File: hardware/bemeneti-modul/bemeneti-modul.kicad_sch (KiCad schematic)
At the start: 0 parts

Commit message: Hardver: bemeneti modul kapcsolási rajz + HDC3020 + buszos táp opció
16 bemenet JST-PH-n (1k + 10k felhúzás + 10 nF, osztó-footprint, ESD),
4 érzékelő-tápcsoport (3,3 / 5 V forrasztható választó + PTC, külön NCP1117),
HDC3020 (saját szimbólum + DEF0008A footprint) + külső I²C PH-csatlakozó.
Modulmag: opcionális buszos táp (D6 + JP2, alapból üres) – D66. ERC: 0 hiba.

Co-Authored-By: Claude Opus 5.5 <noreply@anthropic.com>
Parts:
- added C301, C320: 100n, Capacitor_SMD:C_0603_1608Metric, symbol Device:C
- added C302: 10µ/10V, Capacitor_SMD:C_0805_2012Metric, symbol Device:C
- added C303: 10µ tantál, Capacitor_Tantalum_SMD:CP_EIA-3216-18_Kemet-A, symbol Device:C_Polarized
- added C304, C305, C306, C307: 1µ, Capacitor_SMD:C_0603_1608Metric, symbol Device:C
- added C310, C311, C312, C313, C314, C315, C316, C317, C318, C319, C320, C321, C322, C323, C324, C325: 10n, Capacitor_SMD:C_0603_1608Metric, symbol Device:C
- added F301, F302, F303, F304, F305: PTC 0,2A, Fuse:Fuse_1206_3216Metric, symbol Device:Polyfuse
- added J300: 24V IN, TerminalBlock_Phoenix:TerminalBlock_Phoenix_PT-1,5-2-5.0-H_1x02_P5.00mm_Horizontal, symbol Connector_Generic:Conn_01x02
- added J301: IN0, Connector_JST:JST_PH_B3B-PH-K_1x03_P2.00mm_Vertical, symbol Connector_Generic:Conn_01x03
- added J302: IN1, Connector_JST:JST_PH_B3B-PH-K_1x03_P2.00mm_Vertical, symbol Connector_Generic:Conn_01x03
- added J303: IN2, Connector_JST:JST_PH_B3B-PH-K_1x03_P2.00mm_Vertical, symbol Connector_Generic:Conn_01x03
- added J304: IN3, Connector_JST:JST_PH_B3B-PH-K_1x03_P2.00mm_Vertical, symbol Connector_Generic:Conn_01x03
- added J305: IN4, Connector_JST:JST_PH_B3B-PH-K_1x03_P2.00mm_Vertical, symbol Connector_Generic:Conn_01x03
- added J306: IN5, Connector_JST:JST_PH_B3B-PH-K_1x03_P2.00mm_Vertical, symbol Connector_Generic:Conn_01x03
- added J307: IN6, Connector_JST:JST_PH_B3B-PH-K_1x03_P2.00mm_Vertical, symbol Connector_Generic:Conn_01x03
- added J308: IN7, Connector_JST:JST_PH_B3B-PH-K_1x03_P2.00mm_Vertical, symbol Connector_Generic:Conn_01x03
- added J309: IN8, Connector_JST:JST_PH_B3B-PH-K_1x03_P2.00mm_Vertical, symbol Connector_Generic:Conn_01x03
- added J310: IN9, Connector_JST:JST_PH_B3B-PH-K_1x03_P2.00mm_Vertical, symbol Connector_Generic:Conn_01x03
- added J311: IN10, Connector_JST:JST_PH_B3B-PH-K_1x03_P2.00mm_Vertical, symbol Connector_Generic:Conn_01x03
- added J312: IN11, Connector_JST:JST_PH_B3B-PH-K_1x03_P2.00mm_Vertical, symbol Connector_Generic:Conn_01x03
- added J313: IN12, Connector_JST:JST_PH_B3B-PH-K_1x03_P2.00mm_Vertical, symbol Connector_Generic:Conn_01x03
- added J314: IN13, Connector_JST:JST_PH_B3B-PH-K_1x03_P2.00mm_Vertical, symbol Connector_Generic:Conn_01x03
- added J315: IN14, Connector_JST:JST_PH_B3B-PH-K_1x03_P2.00mm_Vertical, symbol Connector_Generic:Conn_01x03
- added J316: IN15, Connector_JST:JST_PH_B3B-PH-K_1x03_P2.00mm_Vertical, symbol Connector_Generic:Conn_01x03
- added J320: I2C KÜLSŐ, Connector_JST:JST_PH_B4B-PH-K_1x04_P2.00mm_Vertical, symbol Connector_Generic:Conn_01x04
- added JP301: CSOPORT 1, Jumper:SolderJumper-3_P1.3mm_Bridged12_RoundedPad1.0x1.5mm, symbol Jumper:SolderJumper_3_Bridged12
- added JP302: CSOPORT 2, Jumper:SolderJumper-3_P1.3mm_Bridged12_RoundedPad1.0x1.5mm, symbol Jumper:SolderJumper_3_Bridged12
- added JP303: CSOPORT 3, Jumper:SolderJumper-3_P1.3mm_Bridged12_RoundedPad1.0x1.5mm, symbol Jumper:SolderJumper_3_Bridged12
- added JP304: CSOPORT 4, Jumper:SolderJumper-3_P1.3mm_Bridged12_RoundedPad1.0x1.5mm, symbol Jumper:SolderJumper_3_Bridged12
- added R301: 3k3 1%, Resistor_SMD:R_0603_1608Metric, symbol Device:R
- added R302: 10k 1%, Resistor_SMD:R_0603_1608Metric, symbol Device:R
- added R310, R311, R312, R313, R314, R315, R316, R317, R318, R319, R320, R321, R322, R323, R324, R325: 1k, Resistor_SMD:R_0603_1608Metric, symbol Device:R
- added R330, R331, R332, R333, R334, R335, R336, R337, R338, R339, R340, R341, R342, R343, R344, R345, R373: 10k, Resistor_SMD:R_0603_1608Metric, symbol Device:R
- added R350, R351, R352, R353, R354, R355, R356, R357, R358, R359, R360, R361, R362, R363, R364, R365: DNP, Resistor_SMD:R_0603_1608Metric, symbol Device:R
- added R371, R372: 4k7, Resistor_SMD:R_0603_1608Metric, symbol Device:R
- added R374, R375: 100R, Resistor_SMD:R_0603_1608Metric, symbol Device:R
- added U301: NCP1117ST33T3G, Package_TO_SOT_SMD:SOT-223-3_TabPin2, symbol Regulator_Linear:NCP1117-3.3_SOT223
- added U302: HDC3020DEFR, modularis:TI_WSON-8-1EP_2.5x2.5mm_DEF0008A, symbol modularis:HDC3020
- added U303, U304, U305, U306, U307: TPD4E05U06DQAR, Package_SON:USON-10_2.5x1.0mm_P0.5mm, symbol Power_Protection:TPD4E05U06DQA
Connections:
- new net +24V_IN: J300.1 (Pin_1)
- new net +3V3: C320.1, R301.1, R330.1, R331.1, R332.1, R333.1, R334.1, R335.1, R336.1, R337.1, R338.1, R339.1, R340.1, R341.1, R342.1, R343.1, R344.1, R345.1, R371.1, R372.1, R373.1, U302.5 (VDD), U302.6 (~{RESET})
- new net +3V3S: C303.1, F305.1, JP301.1 (A), JP302.1 (A), JP303.1 (A), JP304.1 (A), U301.2 (VO)
- new net +5V: C302.1, JP301.3 (B), JP302.3 (B), JP303.3 (B), JP304.3 (B), U301.3 (VI)
- new net GND: C301.2, C302.2, C303.2, C304.2, C305.2, C306.2, C307.2, C310.2, C311.2, C312.2, C313.2, C314.2, C315.2, C316.2, C317.2, C318.2, C319.2, C320.2, C320.2, C321.2, C322.2, C323.2, C324.2, C325.2, J300.2 (Pin_2), J301.2 (Pin_2), J302.2 (Pin_2), J303.2 (Pin_2), J304.2 (Pin_2), J305.2 (Pin_2), J306.2 (Pin_2), J307.2 (Pin_2), J308.2 (Pin_2), J309.2 (Pin_2), J310.2 (Pin_2), J311.2 (Pin_2), J312.2 (Pin_2), J313.2 (Pin_2), J314.2 (Pin_2), J315.2 (Pin_2), J316.2 (Pin_2), J320.2 (Pin_2), R302.2, R350.2, R351.2, R352.2, R353.2, R354.2, R355.2, R356.2, R357.2, R358.2, R359.2, R360.2, R361.2, R362.2, R363.2, R364.2, R365.2, U301.1 (GND), U302.2 (ADDR), U302.7 (ADDR1), U302.8 (GND), U303.3 (GND), U303.8 (GND), U304.3 (GND), U304.8 (GND), U305.3 (GND), U305.8 (GND), U306.3 (GND), U306.8 (GND), U307.3 (GND), U307.8 (GND)
- new net HDC_ALERT: R373.2, U302.3 (ALERT)
- new net HW_ID: C301.1, R301.2, R302.1
- new net I2C_SCL: R371.2, R374.1, U302.4 (SCL)
- new net I2C_SDA: R372.2, R375.1, U302.1 (SDA)
- new net IN0: C310.1, R310.2, R330.2, R350.1, U303.1 (D1+)
- new net IN0_EXT: J301.3 (Pin_3), R310.1
- new net IN1: C311.1, R311.2, R331.2, R351.1, U303.2 (D1-)
- new net IN10: C320.1, R320.2, R340.2, R360.1, U305.4 (D2+)
- new net IN10_EXT: J311.3 (Pin_3), R320.1
- new net IN11: C321.1, R321.2, R341.2, R361.1, U305.5 (D2-)
- new net IN11_EXT: J312.3 (Pin_3), R321.1
- new net IN12: C322.1, R322.2, R342.2, R362.1, U306.1 (D1+)
- new net IN12_EXT: J313.3 (Pin_3), R322.1
- new net IN13: C323.1, R323.2, R343.2, R363.1, U306.2 (D1-)
- new net IN13_EXT: J314.3 (Pin_3), R323.1
- new net IN14: C324.1, R324.2, R344.2, R364.1, U306.4 (D2+)
- new net IN14_EXT: J315.3 (Pin_3), R324.1
- new net IN15: C325.1, R325.2, R345.2, R365.1, U306.5 (D2-)
- new net IN15_EXT: J316.3 (Pin_3), R325.1
- new net IN1_EXT: J302.3 (Pin_3), R311.1
- new net IN2: C312.1, R312.2, R332.2, R352.1, U303.4 (D2+)
- new net IN2_EXT: J303.3 (Pin_3), R312.1
- new net IN3: C313.1, R313.2, R333.2, R353.1, U303.5 (D2-)
- new net IN3_EXT: J304.3 (Pin_3), R313.1
- new net IN4: C314.1, R314.2, R334.2, R354.1, U304.1 (D1+)
- new net IN4_EXT: J305.3 (Pin_3), R314.1
- new net IN5: C315.1, R315.2, R335.2, R355.1, U304.2 (D1-)
- new net IN5_EXT: J306.3 (Pin_3), R315.1
- new net IN6: C316.1, R316.2, R336.2, R356.1, U304.4 (D2+)
- new net IN6_EXT: J307.3 (Pin_3), R316.1
- new net IN7: C317.1, R317.2, R337.2, R357.1, U304.5 (D2-)
- new net IN7_EXT: J308.3 (Pin_3), R317.1
- new net IN8: C318.1, R318.2, R338.2, R358.1, U305.1 (D1+)
- new net IN8_EXT: J309.3 (Pin_3), R318.1
- new net IN9: C319.1, R319.2, R339.2, R359.1, U305.2 (D1-)
- new net IN9_EXT: J310.3 (Pin_3), R319.1
- new net SCL_EXT: J320.4 (Pin_4), R374.2, U307.1 (D1+)
- new net SDA_EXT: J320.3 (Pin_3), R375.2, U307.2 (D1-)
- new net SUP1: C304.1, F301.2, J301.1 (Pin_1), J302.1 (Pin_1), J303.1 (Pin_1), J304.1 (Pin_1)
- new net SUP1_SEL: F301.1, JP301.2 (C)
- new net SUP2: C305.1, F302.2, J305.1 (Pin_1), J306.1 (Pin_1), J307.1 (Pin_1), J308.1 (Pin_1)
- new net SUP2_SEL: F302.1, JP302.2 (C)
- new net SUP3: C306.1, F303.2, J309.1 (Pin_1), J310.1 (Pin_1), J311.1 (Pin_1), J312.1 (Pin_1)
- new net SUP3_SEL: F303.1, JP303.2 (C)
- new net SUP4: C307.1, F304.2, J313.1 (Pin_1), J314.1 (Pin_1), J315.1 (Pin_1), J316.1 (Pin_1)
- new net SUP4_SEL: F304.1, JP304.2 (C)
- new net SUP_I2C: F305.2, J320.1 (Pin_1)
- no-connect marks 0 -> 29
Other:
- added sheet modulmag (../modulmag/modulmag.kicad_sch)
- note added: "1. ÉRZÉKELŐ-TÁP: külön 3,3 V-os sín (U301, NCP1117) az 5 V-ról – egy zárlatos érzékelő nem indítja újra az MCU-t"
- note added: "2. BEMENETEK (× 16): PH-csatlakozó 1 = táp (SUPk), 2 = GND, 3 = JEL → R_s → MCU-láb; R_fel 3,3 V-ra, R_le (DNP) és C a GND-re, ESD az MCU-oldalon"
- note added: "3. HŐMÉRSÉKLET / PÁRATARTALOM: HDC3020 a NYÁK szélén (alatta és körülötte marás), + 4 tűs PH külső érzékelőhöz (D66)"
- note added: "4 csoport × 4 csatlakozó: csoportonként 3 padas forrasztható választó (alap: 3,3 V; átforrasztva: 5 V) + saját PTC"
- note added: "5 V-os csoportban az érzékelő jele is 5 V lehet: az IN8–IN10 (PA8–PA10) 5 V-tűrő, a többi bemeneten az osztó-footprint kell (R_s 2k2, R_le 3k9, R_fel ki)"
- note added: "Alap: R_s 1k + R_fel 10k + C 10n → érintkező, reed, gomb, open-drain (pl. AH1911), 3,3 V-os kimenet. 12/24 V-os jel: R_s 68k, R_le 10k, R_fel ki."
- note added: "ESD: 4 × TPD4E05U06 – a csatlakozók mellé,"
- note added: "HW-ID: bemeneti modul = 6. sáv (2,48 V)"
- note added: "MODULMAG – A változat, saját 24 V"
- note added: "P78E05 → NCP1117, izolált CAN (D66)"
- note added: "VÁZLAT – generálva a D44/D48/D51/D66 alapján (2026-10-16). Elrendezést rendezd; a bekötés címkékkel kész."
- note added: "a soros R MCU-oldalára"
- title: Általános bemeneti modul (16 bemenet) -> Bemeneti modul – 16 bemenet (JST-PH), 4 érzékelő-tápcsoport, HDC3020, modulmag

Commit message: Hardver: mind az öt kapcsolási rajz elrendezve (vezetékes, blokkos), netlista-ellenőrzővel
Funkcionális blokkok, balról jobbra jelút, tápsín felül / GND alul; blokkon belül
vezeték, blokkok között és az IC-lábakon címke. kigen: lábpozíció, place(),
wire/junction/rail, tükrözés, 1,27 mm-es rács, olvasható mezők. gen/netcmp.py:
két netlista lábszintű összevetése – a bekötés az átrendezés előttivel azonos
(a modulmag D66-os D6/JP2-jét kivéve). ERC: 0 hiba mind az öt lapon.

Co-Authored-By: Claude Opus 5.5 <noreply@anthropic.com>
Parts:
- removed C320: 10n, Capacitor_SMD:C_0603_1608Metric, symbol Device:C
- removed C320: 100n, Capacitor_SMD:C_0603_1608Metric, symbol Device:C
- added C320: 100n, Capacitor_SMD:C_0603_1608Metric, symbol Device:C
- added C320: 10n, Capacitor_SMD:C_0603_1608Metric, symbol Device:C
- U302: Megjegyzés I²C-cím 0x44 (ADDR = ADDR1 = GND); a külső érzékelő más cím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 -> (none)
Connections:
- net +3V3: now also C320.1
- net GND: now also C320.2, C320.2
- net IN10: now also C320.1
- net IN0_EXT: no longer names the net of J301.3 (Pin_3), R310.1
- net IN10_EXT: no longer names the net of J311.3 (Pin_3), R320.1
- net IN11_EXT: no longer names the net of J312.3 (Pin_3), R321.1
- net IN12_EXT: no longer names the net of J313.3 (Pin_3), R322.1
- net IN13_EXT: no longer names the net of J314.3 (Pin_3), R323.1
- net IN14_EXT: no longer names the net of J315.3 (Pin_3), R324.1
- net IN15_EXT: no longer names the net of J316.3 (Pin_3), R325.1
- net IN1_EXT: no longer names the net of J302.3 (Pin_3), R311.1
- net IN2_EXT: no longer names the net of J303.3 (Pin_3), R312.1
- net IN3_EXT: no longer names the net of J304.3 (Pin_3), R313.1
- net IN4_EXT: no longer names the net of J305.3 (Pin_3), R314.1
- net IN5_EXT: no longer names the net of J306.3 (Pin_3), R315.1
- net IN6_EXT: no longer names the net of J307.3 (Pin_3), R316.1
- net IN7_EXT: no longer names the net of J308.3 (Pin_3), R317.1
- net IN8_EXT: no longer names the net of J309.3 (Pin_3), R318.1
- net IN9_EXT: no longer names the net of J310.3 (Pin_3), R319.1
- net SUP1_SEL: no longer names the net of F301.1, JP301.2 (C)
- net SUP2_SEL: no longer names the net of F302.1, JP302.2 (C)
- net SUP3_SEL: no longer names the net of F303.1, JP303.2 (C)
- net SUP4_SEL: no longer names the net of F304.1, JP304.2 (C)
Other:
- note added: "1. ÉRZÉKELŐ-TÁP: külön 3,3 V-os sín (U301, NCP1117) az 5 V-ról – egy zárlatos érzékelő nem indítja újra az MCU-t;"
- note added: "2. BEMENETEK (× 16): PH 1 = táp (SUPk), 2 = GND, 3 = JEL → R_s → csomópont (R_fel a 3,3 V-ra, R_le (DNP) és C a GND-re) → MCU; ESD az MCU-oldalon (lent)"
- note added: "24 V betáp (J300)"
- note added: "3. HŐMÉRSÉKLET / PÁRATARTALOM:"
- note added: "4 csoport × 4 csatlakozó: csoportonként 3 padas forrasztható választó (alap 1–2 = 3,3 V; átforrasztva 2–3 = 5 V) + saját PTC (0,2 A)"
- note added: "5 V-os csoportban az érzékelő jele is 5 V lehet: az IN8–IN10 (PA8–PA10) 5 V-tűrő, a többi bemeneten az osztó-hely kell (R_s 2k2, R_le 3k9, R_fel ki)"
- note added: "= GND); a külső más címen. Az EP lebegve."
- note added: "ESD: 4 × TPD4E05U06 – a csatlakozók mellé, a soros R MCU-oldalára (a soros R korlátozza a magasabb feszültség áramát)"
- note added: "Generálva (hardware/gen/bemeneti-modul.py) – D44/D48/D51/D66 alapján; kézi szerkesztés helyett a generátort módosítsd."
- note added: "HDC3020 a NYÁK szélén (marással) + 4 tűs PH"
- note added: "IN0–IN3"
- note added: "IN12–IN15"
- note added: "IN4–IN7"
- note added: "IN8–IN11"
- note added: "KÜLSŐ I²C (J320)"
- note added: "külső érzékelőhöz (D66). Cím 0x44 (ADDR = ADDR1"
- note removed: "1. ÉRZÉKELŐ-TÁP: külön 3,3 V-os sín (U301, NCP1117) az 5 V-ról – egy zárlatos érzékelő nem indítja újra az MCU-t"
- note removed: "2. BEMENETEK (× 16): PH-csatlakozó 1 = táp (SUPk), 2 = GND, 3 = JEL → R_s → MCU-láb; R_fel 3,3 V-ra, R_le (DNP) és C a GND-re, ESD az MCU-oldalon"
- note removed: "3. HŐMÉRSÉKLET / PÁRATARTALOM: HDC3020 a NYÁK szélén (alatta és körülötte marás), + 4 tűs PH külső érzékelőhöz (D66)"
- note removed: "4 csoport × 4 csatlakozó: csoportonként 3 padas forrasztható választó (alap: 3,3 V; átforrasztva: 5 V) + saját PTC"
- note removed: "5 V-os csoportban az érzékelő jele is 5 V lehet: az IN8–IN10 (PA8–PA10) 5 V-tűrő, a többi bemeneten az osztó-footprint kell (R_s 2k2, R_le 3k9, R_fel ki)"
- note removed: "ESD: 4 × TPD4E05U06 – a csatlakozók mellé,"
- note removed: "VÁZLAT – generálva a D44/D48/D51/D66 alapján (2026-10-16). Elrendezést rendezd; a bekötés címkékkel kész."
- note removed: "a soros R MCU-oldalára"

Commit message: Hardver: kapcsolási rajzok olvashatósága (KiCad MCP vizuális ellenőrzés alapján), output/ gitignore
Co-Authored-By: Claude Opus 5.5 <noreply@anthropic.com>
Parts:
- removed C320: 100n, Capacitor_SMD:C_0603_1608Metric, symbol Device:C
- removed C320: 10n, Capacitor_SMD:C_0603_1608Metric, symbol Device:C
- added C320: 10n, Capacitor_SMD:C_0603_1608Metric, symbol Device:C
- added C320: 100n, Capacitor_SMD:C_0603_1608Metric, symbol Device:C
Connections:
- net +3V3: now also C320.1
- net GND: now also C320.2, C320.2
- net IN10: now also C320.1

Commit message: Hardver: átnézés (C320 javítva), LoRa-előkészítés (D68), bővítők (D69), R6/R7 = 0 Ω (D70)
- bemeneti modul: a HDC3020 hidegítője C330 lett (a C320 kétszer szerepelt);
  a generátor mostantól hibát dob duplikált jelölésre
- vezérlő: E22-900M22S LoRa + u.FL + 74LVC1G04, minden DNP; J8 bővítő (GPIO5),
  7 mérőpont; spec szerinti DNP-k (USB C, 1 MΩ, PMODE, CAN-fojtó + áthidalók);
  saját footprint az LMR36015-höz (RNX) és az E22-höz
- modulmag: HW_REV osztó (PB0), DNP J4 2 × 5 bővítő; relé: DNP SCT-013 → PA0
- mind az öt lap vizuálisan rendbe téve; R6/R7 = 0 Ω
- specek és döntésnapló frissítve (D68–D70)

Co-Authored-By: Claude Opus 5.5 <noreply@anthropic.com>
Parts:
- removed C320: 10n, Capacitor_SMD:C_0603_1608Metric, symbol Device:C
- removed C320: 100n, Capacitor_SMD:C_0603_1608Metric, symbol Device:C
- added C320: 10n, Capacitor_SMD:C_0603_1608Metric, symbol Device:C
- added C330: 100n, Capacitor_SMD:C_0603_1608Metric, symbol Device:C
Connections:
- net +3V3: now also C330.1
- net GND: now also C320.2, C330.2
- net IN10: now also C320.1
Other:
- title: Bemeneti modul – 16 bemenet (JST-PH), 4 érzékelő-tápcsoport, HDC3020, modulmag -> Bemeneti modul – 16 bemenet, 4 tápcsoport, HDC3020

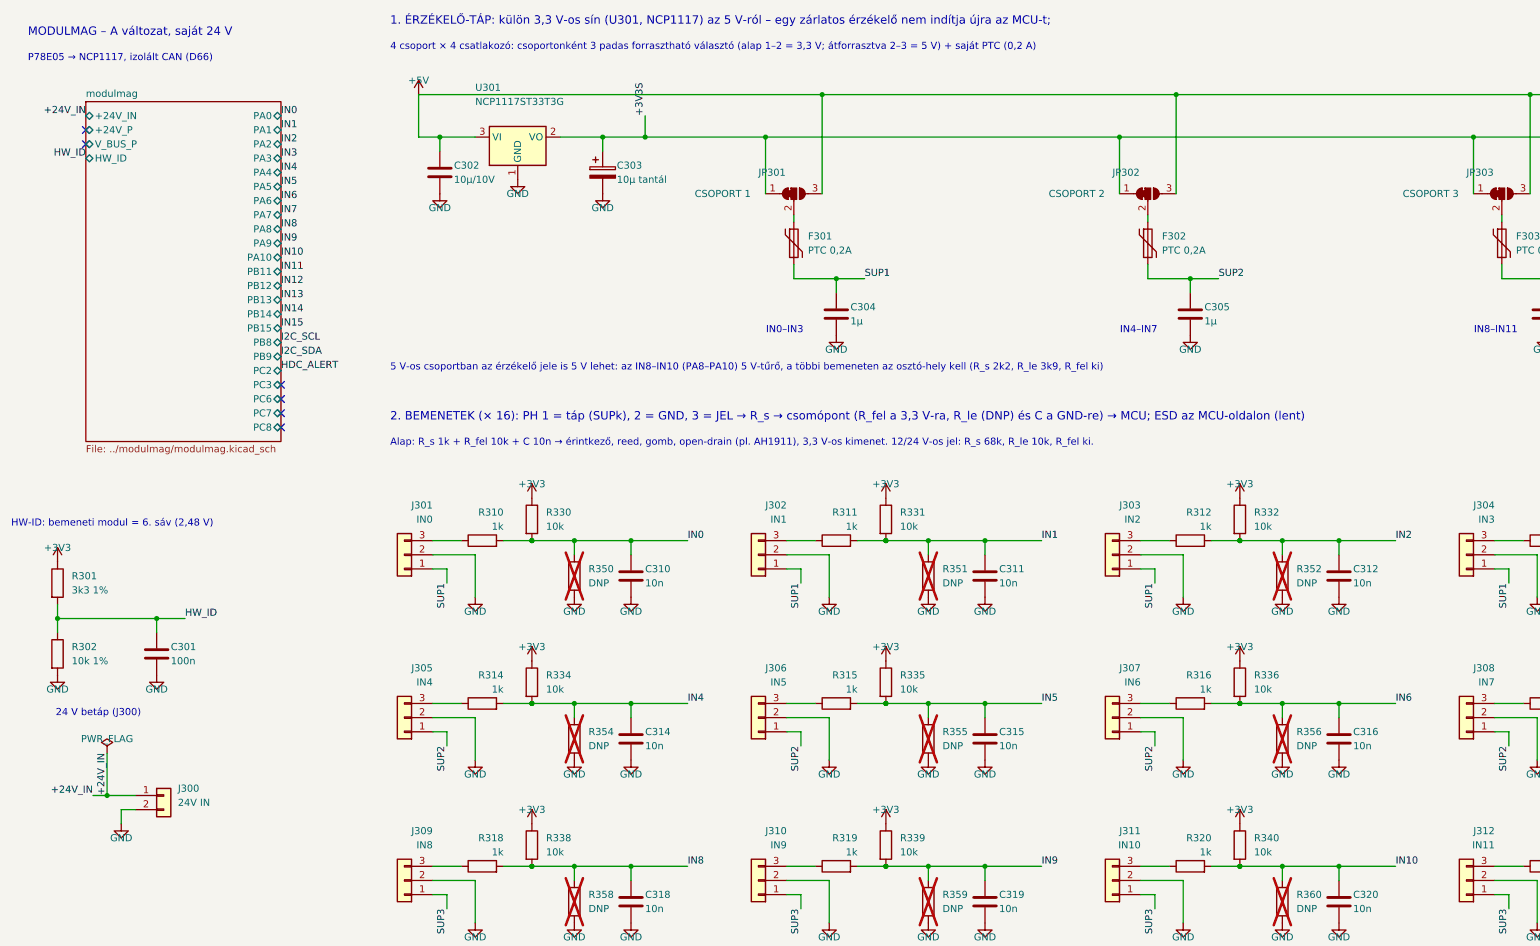
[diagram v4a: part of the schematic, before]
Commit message: Hardver: központi 5 V, közös föld, 12–26 V, HW-ID 16 sáv (D71)
Vezérlő: LMR33630 (5,2 V) + LM66200 (USB-vel VAGY-olva) + TPS259531 eFuse (2 A);
F1 2 A, D1 B360 a 12 V-os működéshez. Modulmag: táp a buszról (AP2112K), TCAN1044AV,
nincs izoláció, PC1 = VBUS_SENSE. LED/relé: VIN_SENSE a PB11-en, relémodul saját
tekercs-táppal. Bemeneti modul: nincs 24 V. HW-ID/HW_REV 16 sáv. Specifikációk,
áttekintés, beszerzés, ütemterv frissítve.

Co-Authored-By: Claude Opus 5.5 <noreply@anthropic.com>
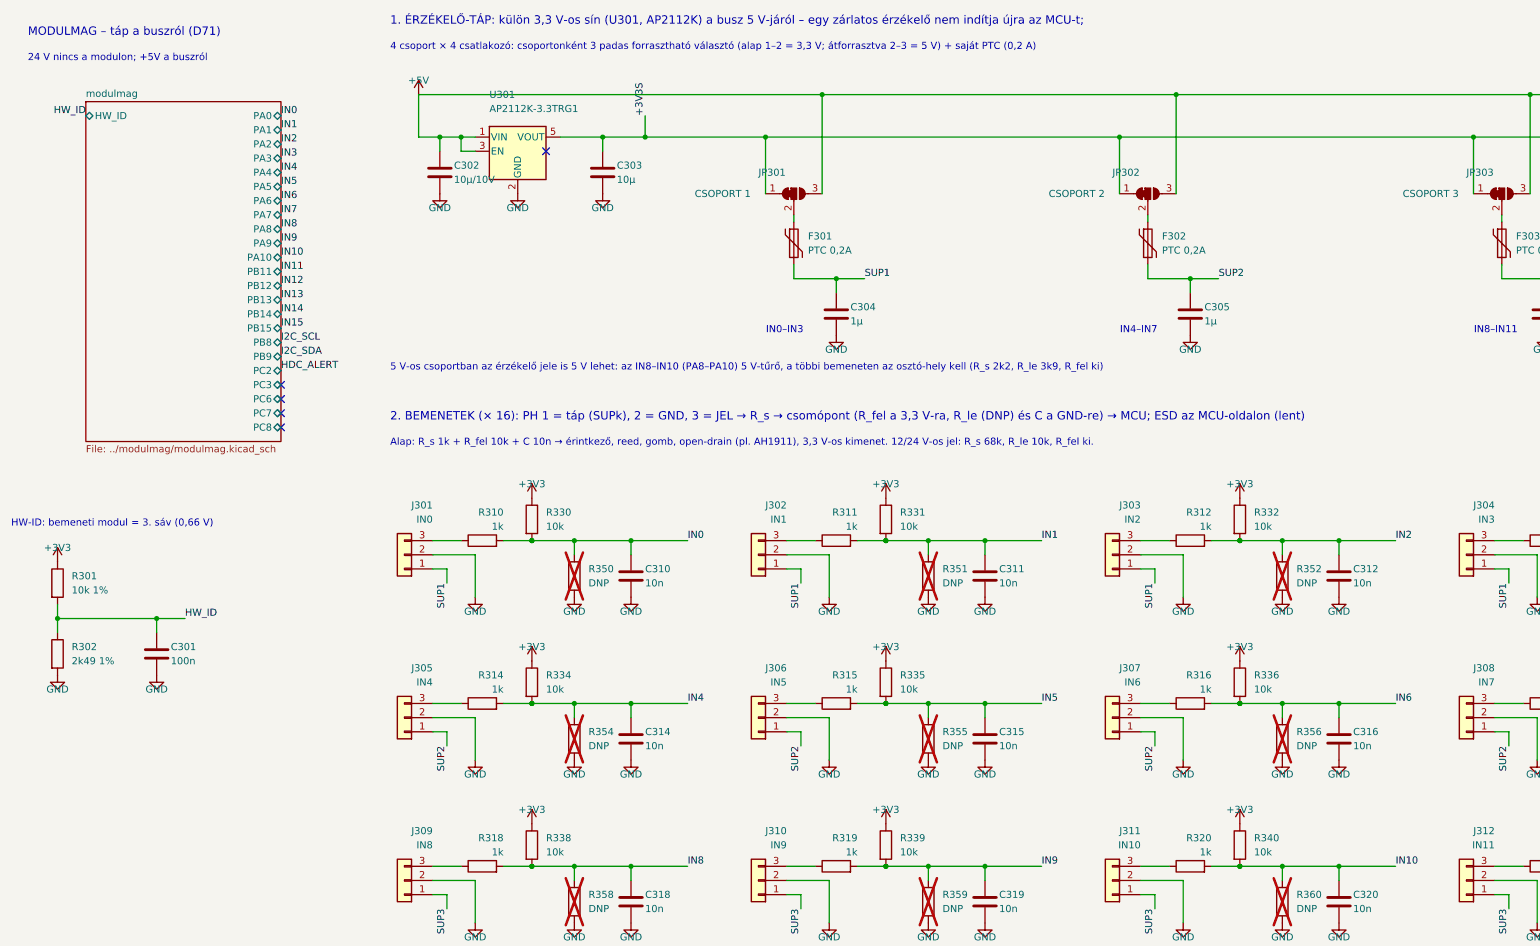
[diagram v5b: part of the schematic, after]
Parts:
- removed C303: 10µ tantál, Capacitor_Tantalum_SMD:CP_EIA-3216-18_Kemet-A, symbol Device:C_Polarized
- removed J300: 24V IN, TerminalBlock_Phoenix:TerminalBlock_Phoenix_PT-1,5-2-5.0-H_1x02_P5.00mm_Horizontal, symbol Connector_Generic:Conn_01x02
- removed U301: NCP1117ST33T3G, Package_TO_SOT_SMD:SOT-223-3_TabPin2, symbol Regulator_Linear:NCP1117-3.3_SOT223
- added C303: 10µ, Capacitor_SMD:C_0805_2012Metric, symbol Device:C
- added U301: AP2112K-3.3TRG1, Package_TO_SOT_SMD:SOT-23-5, symbol Regulator_Linear:AP2112K-3.3
- R301: value 3k3 1% -> 10k 1%
- R302: value 10k 1% -> 2k49 1%
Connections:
- net +3V3S: now also C303.1, U301.5 (VOUT)
- net +5V: now also U301.1 (VIN), U301.3 (EN)
- net GND: now also C303.2, U301.2 (GND)
- no-connect marks 29 -> 28
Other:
- sheet modulmag ports: added none; removed +24V_IN, +24V_P, V_BUS_P
- note added: "1. ÉRZÉKELŐ-TÁP: külön 3,3 V-os sín (U301, AP2112K) a busz 5 V-járól – egy zárlatos érzékelő nem indítja újra az MCU-t;"
- note added: "24 V nincs a modulon; +5V a buszról"
- note added: "HW-ID: bemeneti modul = 3. sáv (0,66 V)"
- note added: "MODULMAG – táp a buszról (D71)"
- note removed: "1. ÉRZÉKELŐ-TÁP: külön 3,3 V-os sín (U301, NCP1117) az 5 V-ról – egy zárlatos érzékelő nem indítja újra az MCU-t;"
- note removed: "24 V betáp (J300)"
- note removed: "HW-ID: bemeneti modul = 6. sáv (2,48 V)"
- note removed: "MODULMAG – A változat, saját 24 V"
- note removed: "P78E05 → NCP1117, izolált CAN (D66)"
